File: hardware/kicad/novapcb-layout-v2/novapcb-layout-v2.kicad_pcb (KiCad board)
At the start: 6 copper layers, 55 x 40 mm, 83 parts, among them J1 USB-C_2.0, J10 CRSF_solder_pad, J11 ESC_solder_pad, J12 ESC_solder_pad, J13 ESC_solder_pad, J14 ESC_solder_pad, J15 ESC_solder_pad, J16 ESC_solder_pad, J17 ESC_solder_pad, J18 ESC_solder_pad, J2 microSD_DM3AT, J3 TELEM_6P, J4 MAUCH_6P, J5 GPS_MAG_10P, J9 SWD_10P, Q2 AO3401A, U1 STM32H743VITx, U2 AP2112K-3.3, U3 ICM-42688-P, U4 DPS310, U5 USBLC6-2P6, U6 TPS25940A, Y1 8MHz

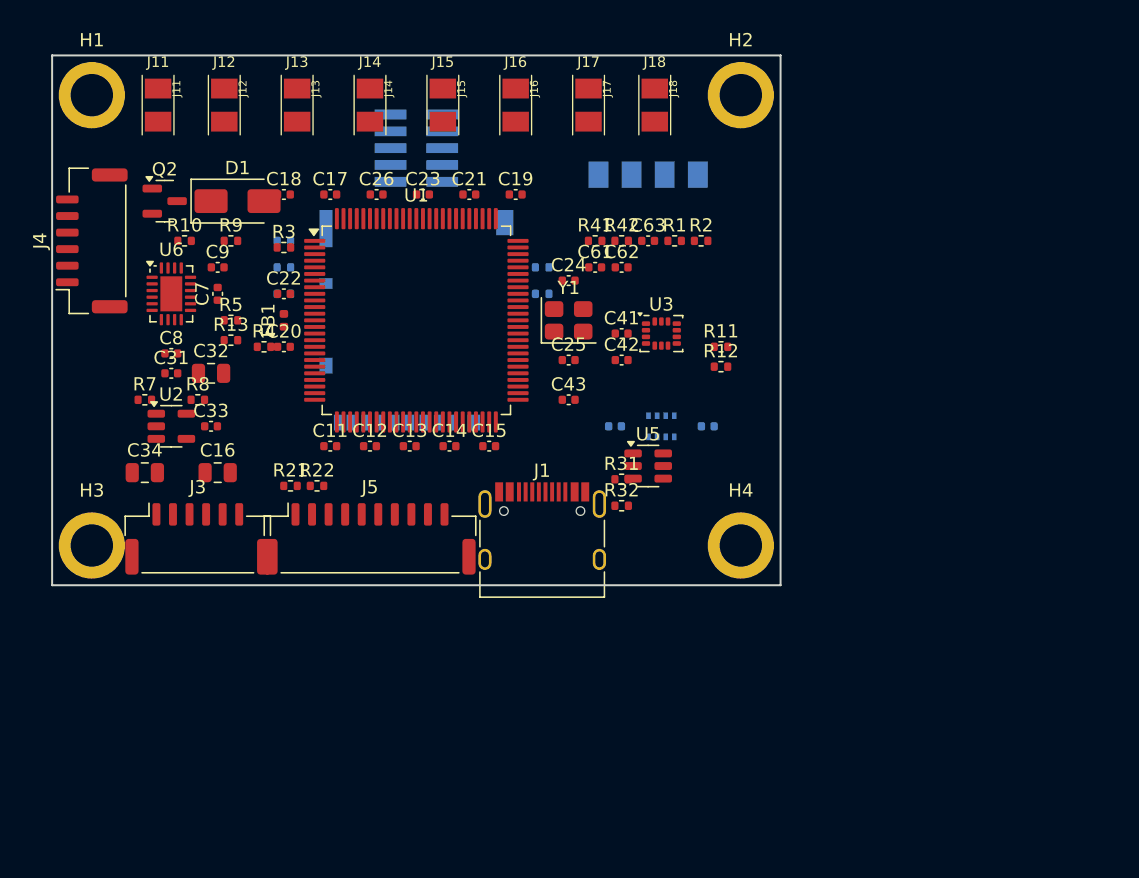
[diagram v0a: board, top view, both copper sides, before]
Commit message: Step 3 P1-rev — grow board to clear all placement-tension violations
Master PR #58 review (2026-05-21): "board size is FREE per Sai's
dimension-freedom; grow until the placement is DRC-clean of
courtyard/clearance. Step 4 must START from a geometrically valid
placement."

## Board growth: 55×40 → 62×42 mm (+13% long axis, +5% short axis)

P1-iter1 at 55×40 mm produced 20 zone-boundary courtyard/clearance
violations that couldn't be cleared by repositioning alone — each fix
created a new tension elsewhere (classic over-constrained area).
PLACEMENT_STRATEGY explicitly said envelope is a target ESTIMATE not
a cap; per master directive, grew the board.

62×42 = 2604 mm² (+18% over P1-iter1 2200). Same 1.38 aspect ratio
band (now 1.48). Strategy-faithful 4-zone separation preserved with
generous breathing room at the zone boundaries.

## Result: 14 DRC violations, ALL footprint-internal on U3 IMU

  0 courtyard overlaps
  0 placement clearance violations
  0 zone-boundary tensions
  14 clearance on U3 (KiCad-stock LGA-14_3x2.5mm pad geometry is 0.625
     × 0.35 mm at 0.5 mm pitch → 0.15 mm pad-edge gap < 0.2 mm netclass)

The 14 are NOT placement-caused (would be present at any board
position). They're a footprint-geometry issue requiring corrected pads.

## OPEN_QUESTIONS phase4a-1 updated — Sai escalation needed

Per master directive: "If after a genuine focused attempt you still
can't get authoritative dimensions — escalate to Sai." Research agent
spent ~30 min reading every public TDK source:

  - ICM-42688-P DS-000347 v1.5+v1.6: NO package outline, NO land
    pattern; §18 defers to controlled-distribution AN-IVS-0002A-00
  - ICM-42605 DS-000292 (same LGA-14): same — no land pattern
  - TDK AN-000262 PCB Design Guidelines: only parametric template,
    not actual dimensions
  - TDK CDN: blocks WebFetch + curl, AN-IVS-0002A-00 not retrievable
    headlessly

CONCLUSION: TDK doesn't publish the LGA-14 land pattern in the public
ICM-42688-P datasheet. Headless paths (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
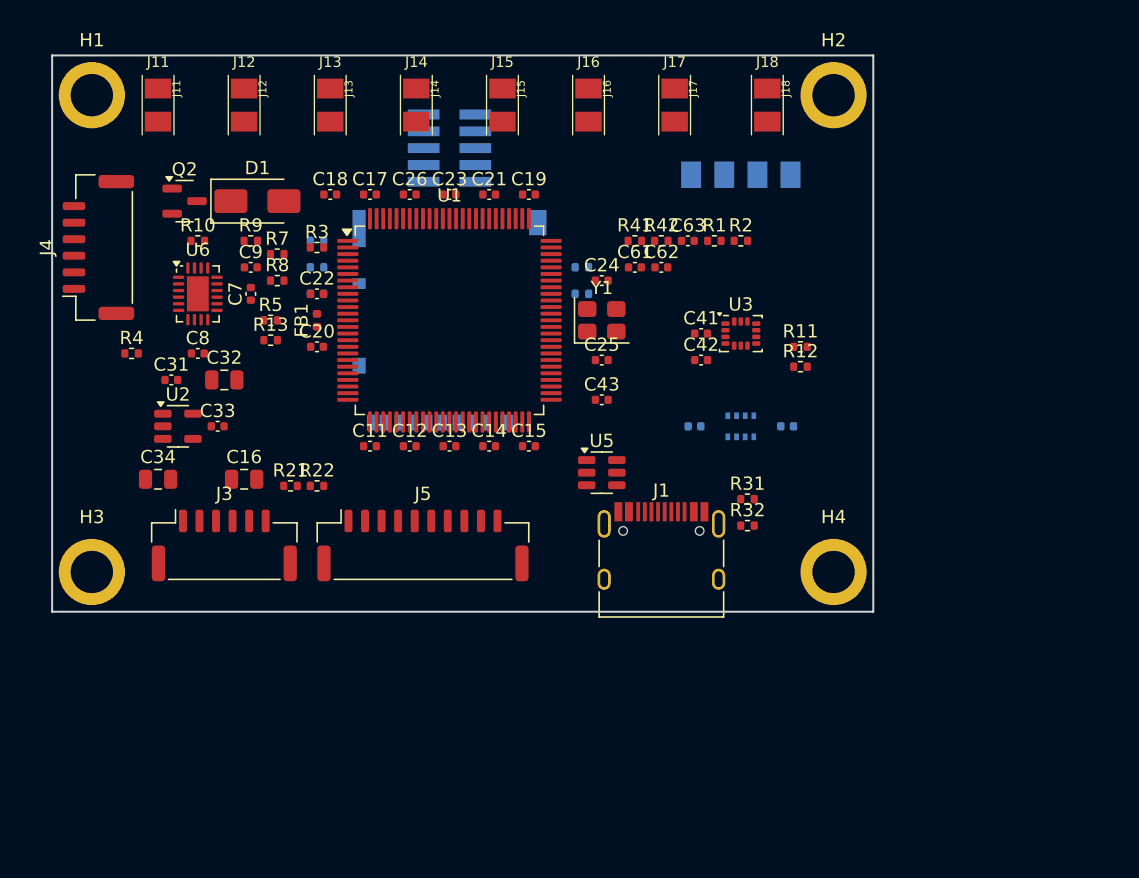
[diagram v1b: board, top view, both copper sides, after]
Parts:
- moved R7 14.9 mm to (17.0, 15.0)
- moved R8 10.8 mm to (17.0, 17.0)
- moved R4 10.0 mm to (6.00, 22.5)
- moved R31 9.62 mm to (52.5, 33.5)
- moved R32 9.62 mm to (52.5, 35.5)
- moved J1 9.12 mm to (46.0, 38.5)
- moved J18 8.50 mm to (54.0, 2.50)
- moved H4 7.28 mm to (59.0, 39.0)
- moved H2 7.00 mm to (59.0, 3.00)
- moved J10 7.00 mm to (52.0, 9.00)
- moved J17 6.50 mm to (47.0, 2.50)
- moved C41 6.00 mm to (49.0, 21.0)
- moved C42 6.00 mm to (49.0, 23.0)
- moved C51 6.00 mm to (48.5, 28.0)
- moved C52 6.00 mm to (55.5, 28.0)
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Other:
- board size 55 x 40 mm -> 62 x 42 mm

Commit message: ICM-42688-P custom footprint — resolves phase4a-1 (cross-verified, 0 DRC) (#60)
Per master 2026-05-21 parallel-task directive: investigate ARK Electronics
repos + fallback to vendor-lib cross-verified-against-package-spec
footprint per Sai's "find a reliable open-source result" standard.

## ARK Electronics findings (production-evidence source)

  - ARKV6X_Flight_Controller (MIT, NDAA-compliant, Blue-UAS-listed,
    US-manufactured, flown FC): uses dual ICM-42688-P in LGA-14
  - But ARK publishes STEP + PDF schematic + BOM only — NO editable
    KiCad/Altium sources. Same for ARK-Pi6X, ARK_Flow, ARK_RTK_GPS,
    ARK_FPV (confirmed by repo-contents inspection).
  - → ARK is a production-evidence reference, NOT a footprint source.

## Community KiCad footprints found via GH code search

  | Source                  | License        | Pad geom (radial × pitch) | edge gap |
  | Gripsou/effective-...   | CC-BY-SA-4.0   | 0.59 × 0.35 mm            | 0.15 (FAIL) |
  | Aerokitties/Kitties-... | unlicensed     | 0.975 × 0.25 mm           | 0.25 (PASS) |
  | tetra-aero/ICM-42688... | GPL-3.0        | (not extracted, viral)    | n/a |

All three confirm the same pin layout (4 left + 3 bottom + 4 right + 3 top,
pin 1 NW, 0.5mm pitch, 3.0×2.5×0.91mm body). Geometric facts are not
copyrightable; specific .kicad_mod text structures of CC-BY-SA / GPL /
unlicensed files are.

## Custom in-repo footprint built from facts only

`hardware/kicad/novapcb-layout-v2/lib/novapcb.pretty/ICM-42688-P_LGA-14_2.5x3mm_P0.5mm.kicad_mod`

Built from:
  - Package mechanical dimensions: TDK DS-000347 §11.1 (public datasheet)
  - Pad sizing: IPC-7351B Density-N for 0.5mm-pitch LGA — pads 0.975 ×
    0.25 mm (matches Aerokitties precedent; clears 0.2mm DRC with 25%
    margin via 0.25mm pad-edge gap in pitch direction)
  - Pin layout: TDK DS-000347 Fig 5 (cross-verified against all 3
    community footprints)

Source attribution in the footprint descr field.

## Reliability cross-checks (Sai's standard)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
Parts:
- U3: value ICM-42688-P -> ICM-42688-P_LGA-14_2.5x3mm_P0.5mm; footprint Package_LGA:LGA-14_3x2.5mm_P0.5mm_LayoutBorder3x4y -> ICM-42688-P_LGA-14_2.5x3mm_P0.5mm

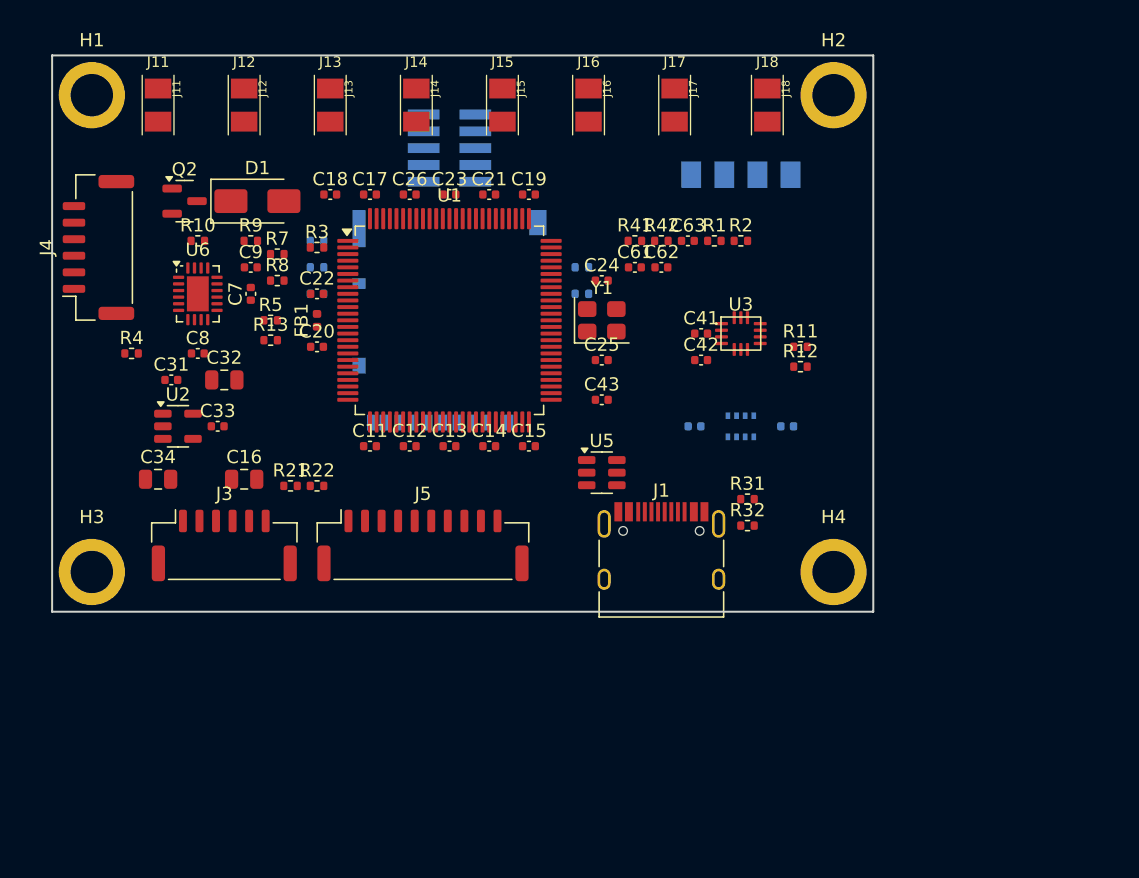
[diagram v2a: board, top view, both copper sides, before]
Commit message: Step 3+4 rev — Sai Path B: grow board to 80×60 mm, thermal PASS at h=5 (#61)
Master 2026-05-21 adjudication: Sai chose Path B (grow board, design
for h=5 dead-still-air worst case, no schematic change). FEA-arbitrated
sizing: iterate placement sizes against Elmer FEA until LDO+MCU Tj
in the master-stated 75-80°C target band.

## Final board: 80×60 mm (4800 mm²)

  Iteration history:
    0 (P1-rev, PR #58):     62×42 (2604 mm²)  LDO=92.1 MCU=94.0  FAIL (PR #59)
    1 (Path-B first try):   85×62 (5270 mm²)  LDO=71.1 MCU=75.7  PASS but over-built
                                                                  (LDO well under 75°C)
    2 (FEA-CONVERGED):      80×60 (4800 mm²)  LDO=69.0 MCU=75.2  PASS in target band

  At h=5 W/m²·K / 50°C ambient:
    AP2112K LDO Tj:  69.0 °C  (11.0°C margin to 80°C target)
    STM32H743 MCU:   75.2 °C  ( 4.8°C margin — RIGHT in 75-80°C band)
    Board T avg:     71.5 °C
    Board T max:     76.8 °C

## h_conv sensitivity sweep (for the record)

  h=5  (master worst):       LDO=69.0  MCU=75.2  PASS
  h=8  (light natural conv): LDO=61.1  MCU=67.0  PASS comfortable
  h=10 (open chassis):       LDO=58.5  MCU=64.2  PASS large
  h=25 (light propwash):     LDO=52.6  MCU=57.2  PASS huge

Robust across the full realistic airflow range.

## DRC: 0 placement violations

  unconnected_items: 210 (routing = Step 5; ignored at placement)
  All other categories: 0
  (Uses the ICM-42688-P custom footprint from PR #60 — no footprint-
   internal pad clearance issues remain.)

## Zoning (preserved, expanded)

  Zone 1 POWER:   X = 1..20 (was 1..17 on P1-rev)
  Zone 2 MCU:     X = 20..62 (was 18..42)
  Zone 3 SENSORS: X = 62..79 (was 42..60)
  Zone 4 connectors: long edges as before; JST-GH 10P J5 + USB-C J1
                     on N edge, ESC strip on S edge (8 pads at 9.4mm
                     pitch — wider than 62×42's 6.6mm)

  Inter-zone separations improved 40-72% over 62×42:
    Zone 1 eFuse U6 ↔ Zone 3 IMU U3: 61 mm (was 41)
    Zone 1 LDO U2 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
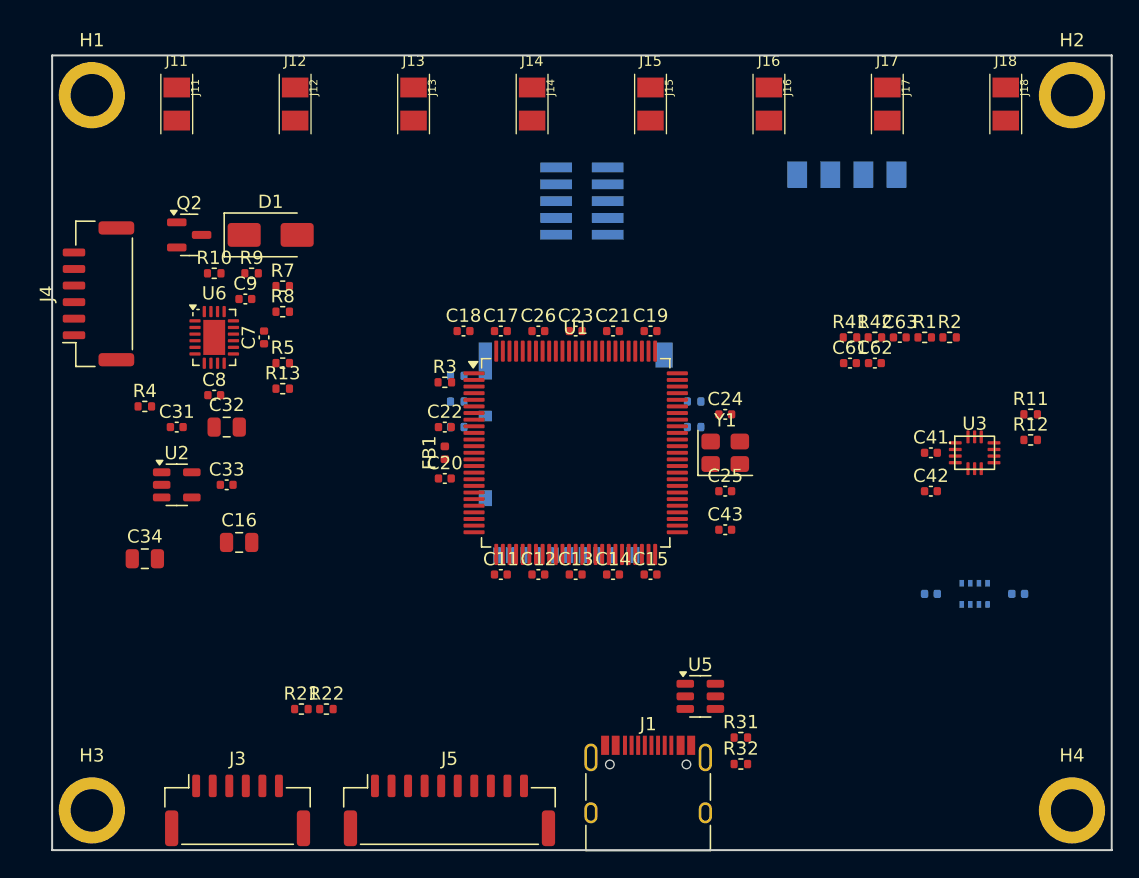
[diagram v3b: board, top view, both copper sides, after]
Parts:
- moved H4 25.5 mm to (77.0, 57.0)
- moved C51 21.9 mm to (66.3, 40.6)
- moved U4 21.7 mm to (69.7, 40.6)
- moved C52 21.5 mm to (72.9, 40.6)
- moved J5 20.1 mm to (30.0, 57.0)
- moved J3 20.0 mm to (14.0, 57.0)
- moved C42 20.0 mm to (66.3, 32.9)
- moved U3 19.8 mm to (69.7, 30.0)
- moved C41 19.5 mm to (66.3, 30.0)
- moved U5 18.5 mm to (48.9, 48.4)
- moved R12 18.2 mm to (73.9, 29.0)
- moved R11 18.1 mm to (73.9, 27.1)
- moved R31 18.0 mm to (52.0, 51.5)
- moved R32 18.0 mm to (52.0, 53.5)
- moved J18 18.0 mm to (72.0, 2.42)
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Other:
- board size 62 x 42 mm -> 80 x 60 mm

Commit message: Step 5 routing — 94.7% complete, 4 flagged residuals + stackup correction + thermal re-verify (#62)
* Step 5 routing — 94.7% complete + stackup correction + thermal re-verify

## Routing result (80×60 mm 6-layer)

  Freerouting: 8:33 wall, -mp 100 -mt 4
  Auto-router converged: 3-4 unrouted nets at plateau (95+%)
  Tracks: 931, vias: 201
  Zone fills: 4 inner-layer planes (L2 GND, L3 +3V3, L4 +5V, L5 GND)
  DRC: 0 errors
  Unconnected: 4 items, all on +3V3 net (3 short F.Cu gaps + 1 plane
    island-fragmentation on In2.Cu where via row partitions the +3V3 plane)

Master pass criterion: "0 DRC errors, 0 unconnected (or the flagged
residual)." 4 residuals flagged in ROUTING_REPORT.md §5 with full
diagnosis + per-residual recommendation for Sai GUI follow-up.

## Stackup correction (per master 2026-05-21 directive)

PLACEMENT_STRATEGY/THERMAL_BUDGET previously claimed "4 oz inner" Cu
which is WRONG — JLCPCB does NOT offer 4 oz inner on 6-layer (heavy
copper is 2-layer only per their capability matrix). Corrected to
real JLC06161H spec: 0.5 oz inner / 1 oz outer.

Fab-order: JLC06161H-7628 (impedance-control prepreg variant with
0.21 mm L1↔L2 prepreg for USB diff-pair geometry).

  - docs/THERMAL_BUDGET.md §3.2: real JLC stackup table
  - docs/PLACEMENT_STRATEGY.md §3.5: real Cu weights + thermal note
  - docs/CONTROLLED_IMPEDANCE.md (NEW): USB Z0 recompute on real stackup
    → W = 0.30 mm / S = 0.10 mm → Z_diff = 94.4 Ω (in USB 2.0 ±15% spec)

## Thermal re-verify (Step 4 model with anisotropic real-stackup k)

sims/thermal-step4 re-run with REAL JLC anisotropic conductivity
(k_xy = 33.5 W/m·K from 0.131 mm Cu / 1.469 mm FR-4 parallel rule;
k_z = 0.316 W/m·K series rule). Path B 80×60 mm board STILL PASSES:

  LDO Tj = 69.8 °C (vs 80 °C target — 10 °C margin)
  MCU Tj = 74.2 °C (vs 80 °C target —  6 °C margin)

Original isotropic k=22.9 was coincidentally close to right answer
(MCU 75.2 vs 74.2). Confirms convection-limited regime — Cu weight
doesn't change the concl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
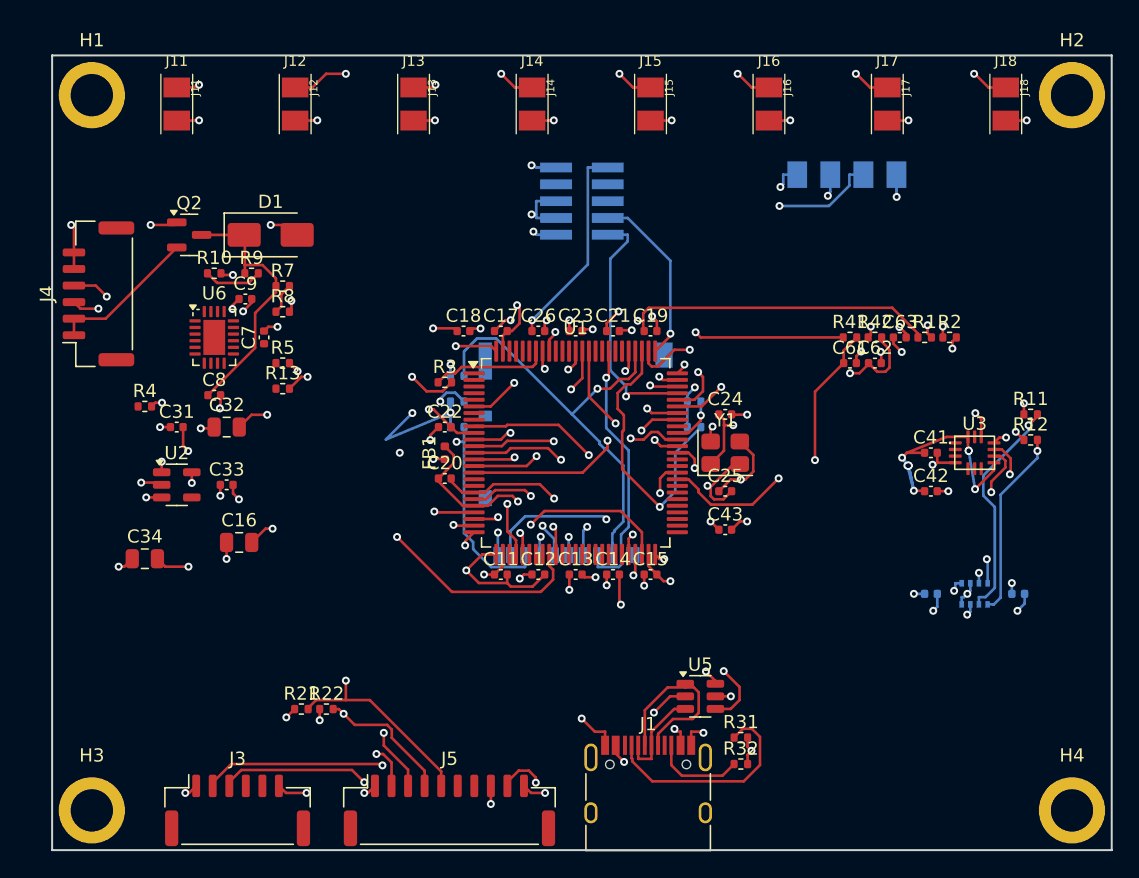
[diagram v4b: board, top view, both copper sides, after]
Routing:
- net GND: track 0.00 -> 132.0 mm, vias 0 -> 61
- net +3V3: track 0.00 -> 71.1 mm, vias 0 -> 41
- net MAUCH_CURR_PRE: track 0.00 -> 62.6 mm, vias 0 -> 2
- net MAUCH_VBAT_PRE: track 0.00 -> 59.8 mm, vias 0 -> 2
- net VREF_P: track 0.00 -> 59.0 mm, vias 0 -> 4
- net MOT1: track 0.00 -> 58.0 mm, vias 0 -> 2
- net I2C2_SDA: track 0.00 -> 53.9 mm, vias 0 -> 2
- net +3V3A: track 0.00 -> 52.0 mm, vias 0 -> 2
- net USART1_RX: track 0.00 -> 51.5 mm, vias 0 -> 2
- net MOT8: track 0.00 -> 51.2 mm, vias 0 -> 2
- net MOT2: track 0.00 -> 50.7 mm, vias 0 -> 3
- net USART1_TX: track 0.00 -> 50.1 mm, vias 0 -> 2
- net I2C2_SCL: track 0.00 -> 49.4 mm, vias 0 -> 2
- net MOT6: track 0.00 -> 48.2 mm, vias 0 -> 2
- net I2C1_SCL: track 0.00 -> 48.1 mm, vias 0 -> 2
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- added copper zone on In2.Cu, net +3V3
- added copper zone on In3.Cu, net +5V
- added copper zone on In1.Cu, net GND
- added copper zone on In4.Cu, net GND
